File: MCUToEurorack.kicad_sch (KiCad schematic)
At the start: 27 parts, among them J1 MCUToAudio1, J2 MCUToAudio1, J3 MCUToAudio2, J4 MCUToAudio2, J5 MCUToCV1, J6 MCUToCV1, J7 MCUToCV2, J8 MCUToCV2, U2 TL074

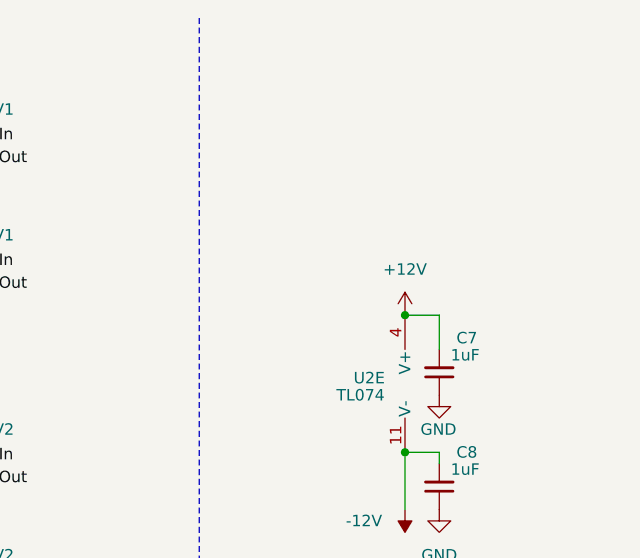
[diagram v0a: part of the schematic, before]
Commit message: Layout tweaks
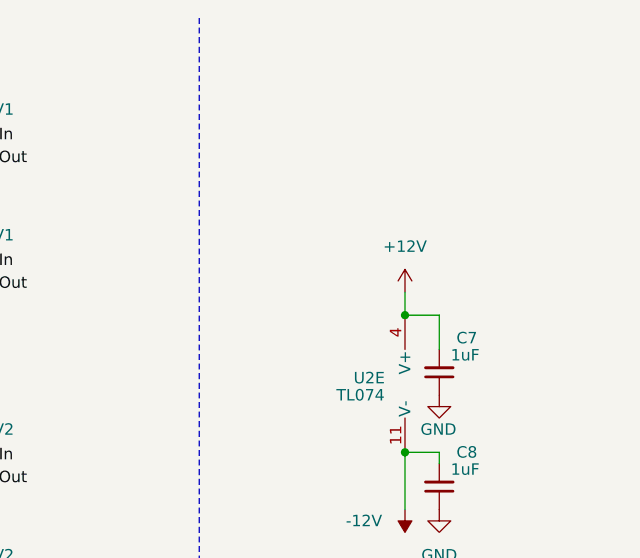
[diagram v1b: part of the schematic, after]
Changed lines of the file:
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@@
+    (stroke (width 0) (type default))
+  )
+  (wire (pts (xy 260.35 43.18) (xy 260.35 45.72))
     (stroke (width 0) (type default))
   )
@@
     )
   )
-  (symbol (lib_id "power:+12V") (at 260.35 45.72 0) (unit 1)
+  (symbol (lib_id "power:+12V") (at 260.35 43.18 0) (unit 1)
     (in_bom yes) (on_board yes) (dnp no) (fields_autoplaced)
-    (property "Reference" "#PWR011" (at 260.35 49.53 0)
-      (effects (font (size 1.27 1.27)) hide)
-    )
-    (property "Value" "+12V" (at 260.35 40.64 0)
-      (effects (font (size 1.27 1.27)))
-    )
-    (property "Footprint" "" (at 260.35 45.72 0)
-      (effects (font (size 1.27 1.27)) hide)
-    )
-    (property "Datasheet" "" (at 260.35 45.72 0)
-      (effects (font (size 1.27 1.27)) hide)
-    )
+    (property "Reference" "#PWR011" (at 260.35 46.99 0)
+      (effects (font (size 1.27 1.27)) hide)
+    )
+    (property "Value" "+12V" (at 260.35 38.1 0)
+      (effects (font (size 1.27 1.27)))
+    )
+    (property "Footprint" "" (at 260.35 43.18 0)
+      (effects (font (size 1.27 1.27)) hide)
+    )
+    (property "Datasheet" "" (at 260.35 43.18 0)
+      (effects (font (size 1.27 1.27)) hide)
+    )
